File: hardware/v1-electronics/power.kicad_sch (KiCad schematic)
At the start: 33 parts, among them IC3 USBLC6-2SC6, IC4 TPS61288LRQQR, IC5 MP2721GRH-0000-Z, J1 USB_C_Receptacle_USB2.0_14P, J4 Conn_01x02, SW77 SW_Push

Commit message: feat(v1 hardware): select passives values
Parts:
- removed C54: C_Small, symbol Device:C_Small
- added C55: 0.10μF, symbol Device:C_Small
- added C56, C57: 22μF, symbol Device:C_Small
- C27: value 1uF -> 1μF
- C31: value 4.7uF -> 4.7μF
- C34, C48: value 20uF -> 20μF
- C47: value 1uF -> 10μF
- C49: value C_Small -> 0.10μF
- C50: value C_Small -> 10μF
- C51: value C_Small -> 2.20μF
- C52: value C_Small -> 22μF
- C53: value C_Small -> 2.7nF
- L3: value L_Ferrite_Small -> 2.20μH
- L4: value L_Small -> 560nH
- R47, R48: value 5.1k -> 5.1kΩ
- R49, R50, R51, R55: value 10k -> 10kΩ
- R52: value R_Small -> 6kΩ
- R53: value R_Small -> 44kΩ
- R54: value R_Small -> 10kΩ
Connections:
- net V_CHRG is gone; now on net V_IN_TPS: L4.1
- net COMP: now also C53.2; no longer C53.1
- net Earth: now also C55.1, C56.1, C57.1
- net at R54.1: now also C53.1; no longer C53.2
- net V_IN_TPS: now reaches C34.1, C50.2, IC4.7 (VIN), IC5.13 (SYS)
- net V_IN_TPS: now also L3.2, C55.2; no longer L3.1
- net BST_TPS: now reaches IC4.8 (BST)
- net BST_TPS: now also C49.2; no longer C49.1
- net SW_TPS: now reaches IC4.9 (SW_2)
- net SW_TPS: now also C49.1, IC4.4 (SW_1), L3.1
- net BST renamed BST_MP
- net SW renamed SW_MP
- net VOUT renamed V_OUT
- net V_OUT: now also C56.2, C57.2
- no-connect marks 1 -> 0
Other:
- note added: "Did a bunch of math to select a part for this. It resulted in me going with the recommended inductance"
- note added: "Did the math, realized I don't have control system intuition. I have raw values I need to map to stardard resistor and capcitor size and values: - R_C = 14403.29218 Ω - C_C = 2.673 nF - C_P = 6.4152 pF These are the values after plugging in a real output cap (CL21A226MAQNNN): - R_C = 10020.57613 Ω - C_C = 2.673 nF - C_P = 2.88684 pF These are the standard values I'm going with: - R_C = 10 kΩ - C_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"
- note added: "Have not done the math for this yet This involves control theory noise a big issue in these system"
- note added: "Not sure if I should put a capacitor here. TI recommends putting a capacitor across the second resistor(R2) to protect against noise. The criteria is whiether R2 > or < 15kΩ. Though the datasheet has confliciting suggestions between Section 9.2.2.1 and Section 9.2"
- note added: "Set V_out to 5v Datasheet Section 9.2.2.1"
- note added: "This cap needs to be rated for +4A, X7R or X5R of current based on the page 40 of the datasheet. I caculated a max current ripple of about 1.3A"
- note added: "You should use the TPS61288L HotRod Lite variant"
- note added: "based on Datasheet Section 9.2.2.4 used to manage: - voltage ripple - load transient response Watch out for DC Bias injection **optional review **derating is important here Choose this cap: CL21A226MAQNNN"
- note added: "calculations the value of the inductor for our usage is about 509 nH, for part finding perposes 560 nH part."
- moved on the sheet: C46, C47, C49, C53, L3, L4, R52, R53, R54

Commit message: refactor(v1 hardware): convert switch matrix to hierarchical pins
made other changes
had claude generate a script for making the convertion
the references for this file still need to be fixed
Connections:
- net Earth renamed PGND
- net GND renamed DGND
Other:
- title: (none) -> Slack
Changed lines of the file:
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@@
 	(generator_version "10.0")
 	(paper "User" 510 300)
+	(title_block
+		(title "Slack")
+		(date "2026-06-17")
+		(rev "A.0.0")
+	)
 	(rectangle
 		(start 228.6 149.86)
@@
 	)
 	(junction
+		(at 487.68 86.36)
+		(diameter 0)
+		(color 0 0 0 0)
+	)
+	(junction
 		(at 452.12 88.9)
 		(diameter 1.5)
@@
 	)
 	(junction
+		(at 172.72 96.52)
+		(diameter 1.5)
+		(color 0 0 0 0)
+	)
+	(junction
 		(at 299.72 193.04)
 		(diameter 0)
@@
 	(wire
 		(pts
+			(xy 172.72 93.98) (xy 172.72 96.52)
+		)
+		(stroke
+			(width 0.5)
+			(type default)
+		)
+	)
+	(wire
+		(pts
 			(xy 365.76 177.8) (xy 368.3 177.8)
 		)
@@
 	(wire
 		(pts
+			(xy 490.22 86.36) (xy 487.68 86.36)
+		)
+		(stroke
+			(width 0.5)
+			(type default)
+		)
+	)
+	(wire
+		(pts
 			(xy 304.8 167.64) (xy 314.96 167.64)
 		)
@@
 	(wire
 		(pts
+			(xy 487.68 86.36) (xy 487.68 88.9)
+		)
+		(stroke
+			(width 0.5)
+			(type default)
+		)
+	)
+	(wire
+		(pts
 			(xy 457.2 91.44) (xy 457.2 88.9)
 		)
@@
 	(wire
 		(pts
-			(xy 487.68 83.82) (xy 487.68 88.9)
+			(xy 487.68 83.82) (xy 487.68 86.36)
 		)
 		(stroke
@@
 	(wire
 		(pts
-			(xy 50.8 96.52) (xy 251.46 96.52)
+			(xy 50.8 96.52) (xy 172.72 96.52)
 		)
 		(stroke
@@
 	(wire
 		(pts
+			(xy 172.72 96.52) (xy 251.46 96.52)
+		)
+		(stroke
+			(width 0.5)
+			(type default)
+		)
+	)
+	(wire
+		(pts
 			(xy 106.68 66.04) (xy 104.14 66.04)
 		)
@@
 		)
 	)
-	(label "V_BUS"
-		(at 58.42 96.52 0)
-		(effects
-			(font
-				(size 1.27 1.27)
-			)
-			(justify left bottom)
-		)
-	)
 	(label "BST_MP"
 		(at 284.48 99.06 0)
@@
 		)
 	)
-	(global_label "D-"
-		(shape input)
-		(at 165.1 106.68 270)
-		(fields_autoplaced yes)
-		(effects
-			(font
-				(size 1.27 1.27)
-			)
-			(justify right)
-		)
-		(property "Intersheetrefs" "${INTERSHEET_REFS}"
-			(at 165.1 112.5076 90)
-			(hide yes)
-			(show_name no)
-			(do_not_autoplace no)
-			(effects
-				(font
-					(size 1.27 1.27)
-				)
-				(justify right)
-			)
-		)
-	)
 	(global_label "I2C1_SCL"
 		(shape input)
@@
 		)
 	)
-	(global_label "D+"
-		(shape input)
-		(at 160.02 106.68 270)
-		(fields_autoplaced yes)
-		(effects
-			(font
-				(size 1.27 1.27)
-			)
-			(justify right)
-		)
-		(property "Intersheetrefs" "${INTERSHEET_REFS}"
-			(at 160.02 112.5076 90)
-			(hide yes)
-			(show_name no)
-			(do_not_autoplace no)
-			(effects
-				(font
-					(size 1.27 1.27)
-				)
-				(justify right)
-			)
-		)
-	)
 	(global_label "I2C1_SDA"
 		(shape input)
@@
 		)
 	)
+	(hierarchical_label "V_BUS"
+		(shape output)
+		(at 172.72 93.98 90)
+		(effects
+			(font
+				(size 1.27 1.27)
+			)
+			(justify left)
+		)
+	)
+	(hierarchical_label "V_SYS"
+		(shape output)
+		(at 490.22 86.36 0)
+		(effects
+			(font
+				(size 1.27 1.27)
+			)
+			(justify left)
+		)
+	)
+	(hierarchical_label "D+"
+		(shape bidirectional)
+		(at 160.02 106.68 270)
+		(effects
+			(font
+				(size 1.27 1.27)
+			)
+			(justify right)
+		)
+	)
+	(hierarchical_label "D-"
+		(shape bidirectional)
+		(at 165.1 106.68 270)
+		(effects
+			(font
+				(size 1.27 1.27)
+			)
+			(justify right)
+		)
+	)
 	(symbol
 		(lib_id "Device:L_Small")
@@
 			)
 		)
-		(property "Value" "Earth"
+		(property "Value" "PGND"
 			(at 370.84 114.3 0)
 			(show_name no)
@@
 			)
 		)
-		(property "Value" "GND"
+		(property "Value" "DGND"
 			(at 35.5599 138.43 0)
 			(show_name no)
@@
 			)
 		)
-		(property "Value" "Earth"
+		(property "Value" "PGND"
 			(at 269.24 226.06 0)
 			(show_name no)
@@
 			)
 		)
-		(property "Value" "GND"
+		(property "Value" "DGND"
 			(at 271.78 137.16 0)
 			(show_name no)
@@
 			)
 		)
-		(property "Value" "Earth"
+		(property "Value" "PGND"
 			(at 477.52 101.6 0)
 			(show_name no)
@@
 			)
 		)
-		(property "Value" "GND"
+		(property "Value" "DGND"
 			(at 414.02 127 0)
 			(show_name no)
@@
 			)
 		)
-		(property "Value" "GND"
+		(property "Value" "DGND"
 			(at 50.8 156.2099 0)
 			(show_name no)
@@
 			)
 		)
-		(property "Value" "Earth"
+		(property "Value" "PGND"
 			(at 274.32 142.24 0)
 			(show_name no)
@@
 			)
 		)
-		(property "Value" "GND"
+		(property "Value" "DGND"
 			(at 88.8999 87.63 0)
 			(show_name no)
@@
 			)
 		)
-		(property "Value" "Earth"
+		(property "Value" "PGND"
 			(at 457.2 101.6 0)
 			(show_name no)
@@
 			)
 		)
-		(property "Value" "Earth"
+		(property "Value" "PGND"
 			(at 314.96 200.66 0)
 			(show_name no)
@@
 			)
 		)
-		(property "Value" "GND"
+		(property "Value" "DGND"
 			(at 294.64 180.34 0)
 			(show_name no)
@@
 			)
 		)
-		(property "Value" "Earth"
+		(property "Value" "PGND"
 			(at 467.36 101.6 0)
 			(show_name no)
@@
 			)
 		)
-		(property "Value" "Earth"
+		(property "Value" "PGND"
 			(at 396.24 114.3 0)
 			(show_name no)
@@
 			)
 		)
-		(property "Value" "GND"
+		(property "Value" "DGND"
 			(at 426.72 121.92 0)
 			(show_name no)
@@
 			)
 		)
-		(property "Value" "Earth"
+		(property "Value" "PGND"
 			(at 299.72 203.2 0)
 			(show_name no)
@@
 			)
 		)
-		(property "Value" "Earth"
+		(property "Value" "PGND"
 			(at 309.88 114.3 0)
 			(show_name no)
@@
 			)
 		)
-		(property "Value" "GND"
+		(property "Value" "DGND"
 			(at 441.96 175.26 0)
 			(show_name no)
@@
 			)
 		)
-		(property "Value" "GND"
+		(property "Value" "DGND"
 			(at 281.94 199.3899 0)
 			(show_name no)
@@
 			)
 		)
-		(property "Value" "GND"
+		(property "Value" "DGND"
 			(at 403.86 182.88 0)
 			(show_name no)
@@
 			)
 		)
-		(property "Value" "Earth"
+		(property "Value" "PGND"
 			(at 419.1 121.92 0)
 			(show_name no)
@@
 			)
 		)
-		(property "Value" "GND"
+		(property "Value" "DGND"
 			(at 243.84 214.6299 0)
 			(show_name no)
@@
 			)
 		)
-		(property "Value" "Earth"
+		(property "Value" "PGND"
 			(at 266.7 180.34 0)
 			(show_name no)
@@
 			)
 		)
-		(property "Value" "GND"
+		(property "Value" "DGND"
 			(at 27.9399 138.43 0)
 			(show_name no)

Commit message: refactor(v1 hardware): all sheets now use hierarchical labels
We'll might change these to buses down the line, but we'll see
I'm happy for now
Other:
- note added: "SHould this be on PGND?"
- note removed: "Input Decoupler"
- moved on the sheet: C47

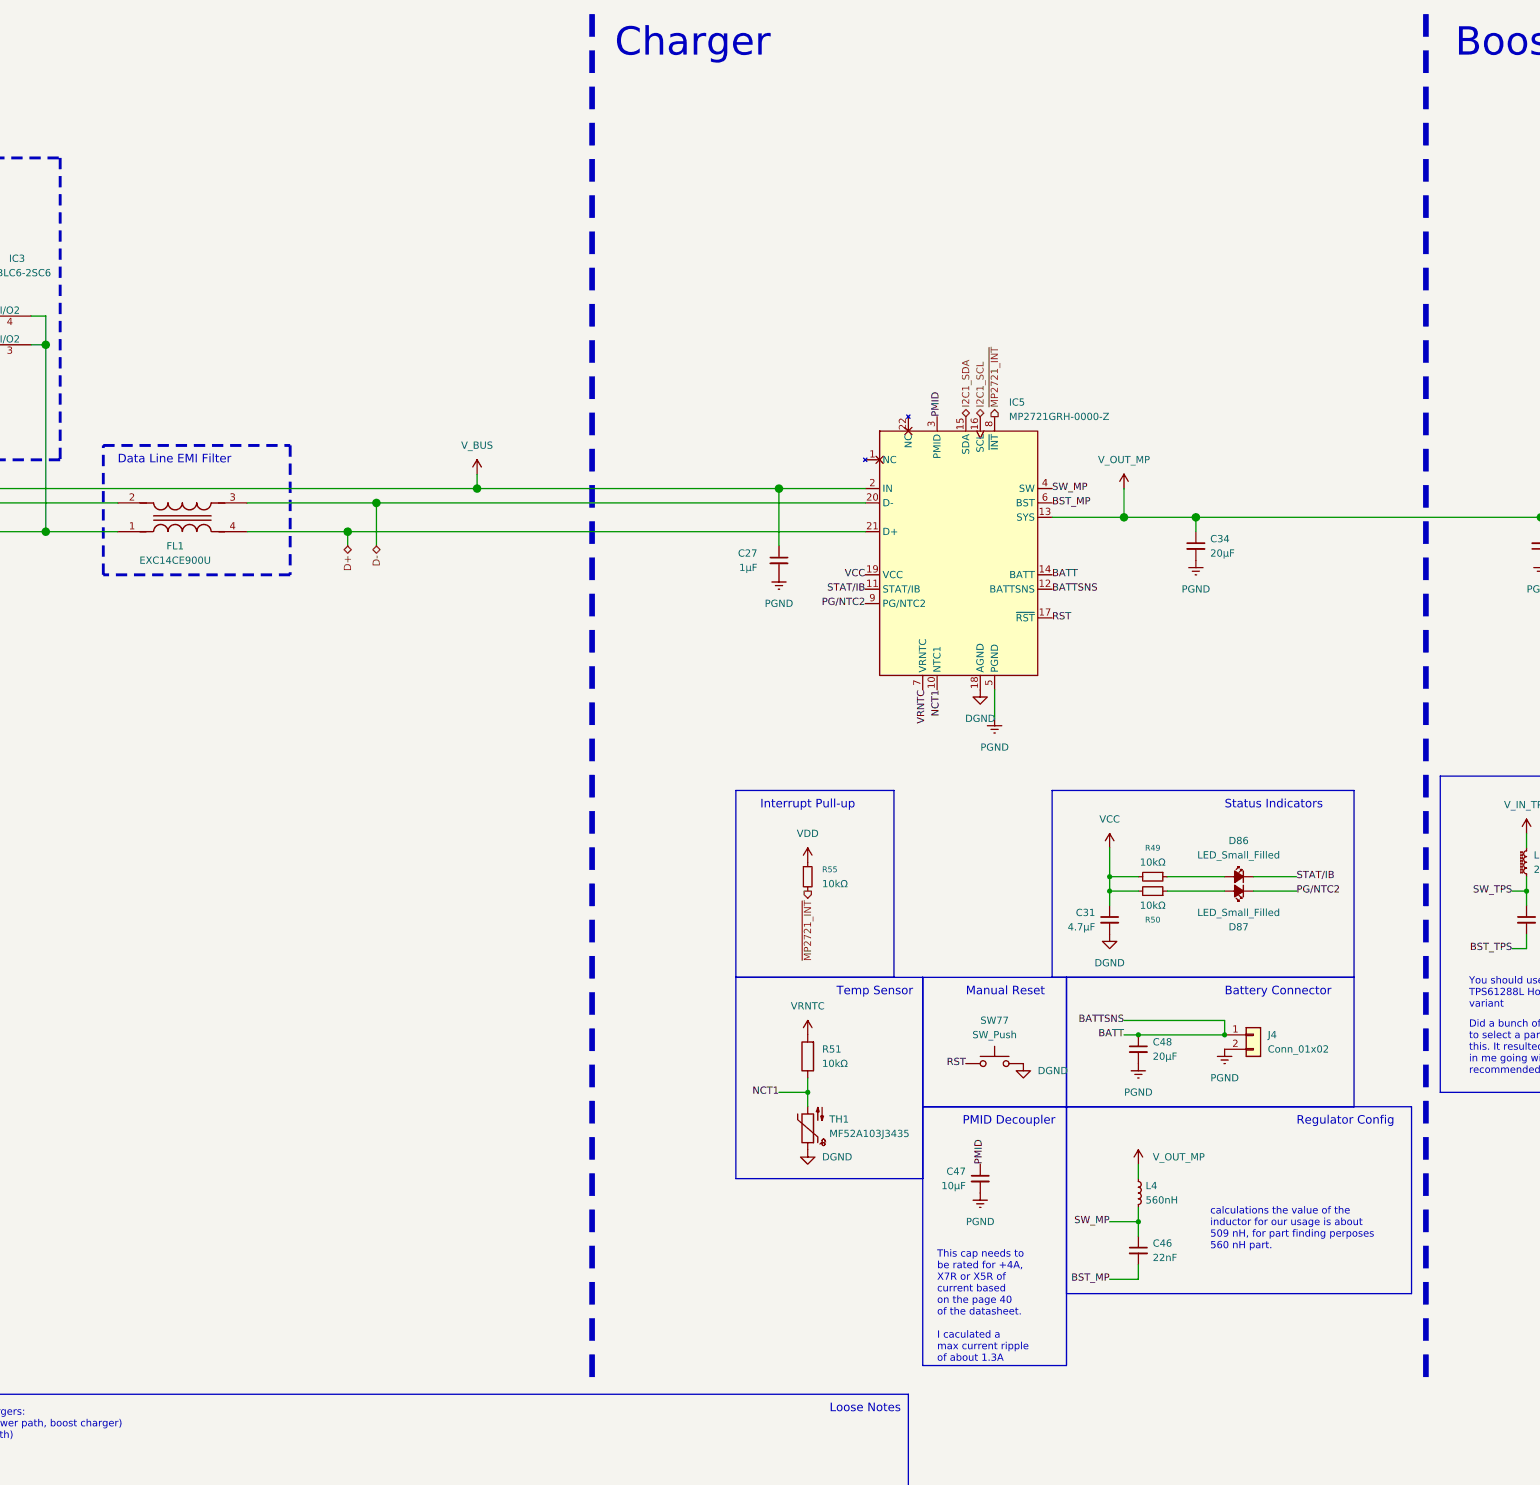
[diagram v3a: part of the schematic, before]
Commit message: refactor(v1 hardware): root level schematic is made discriptive with hierarchical pins
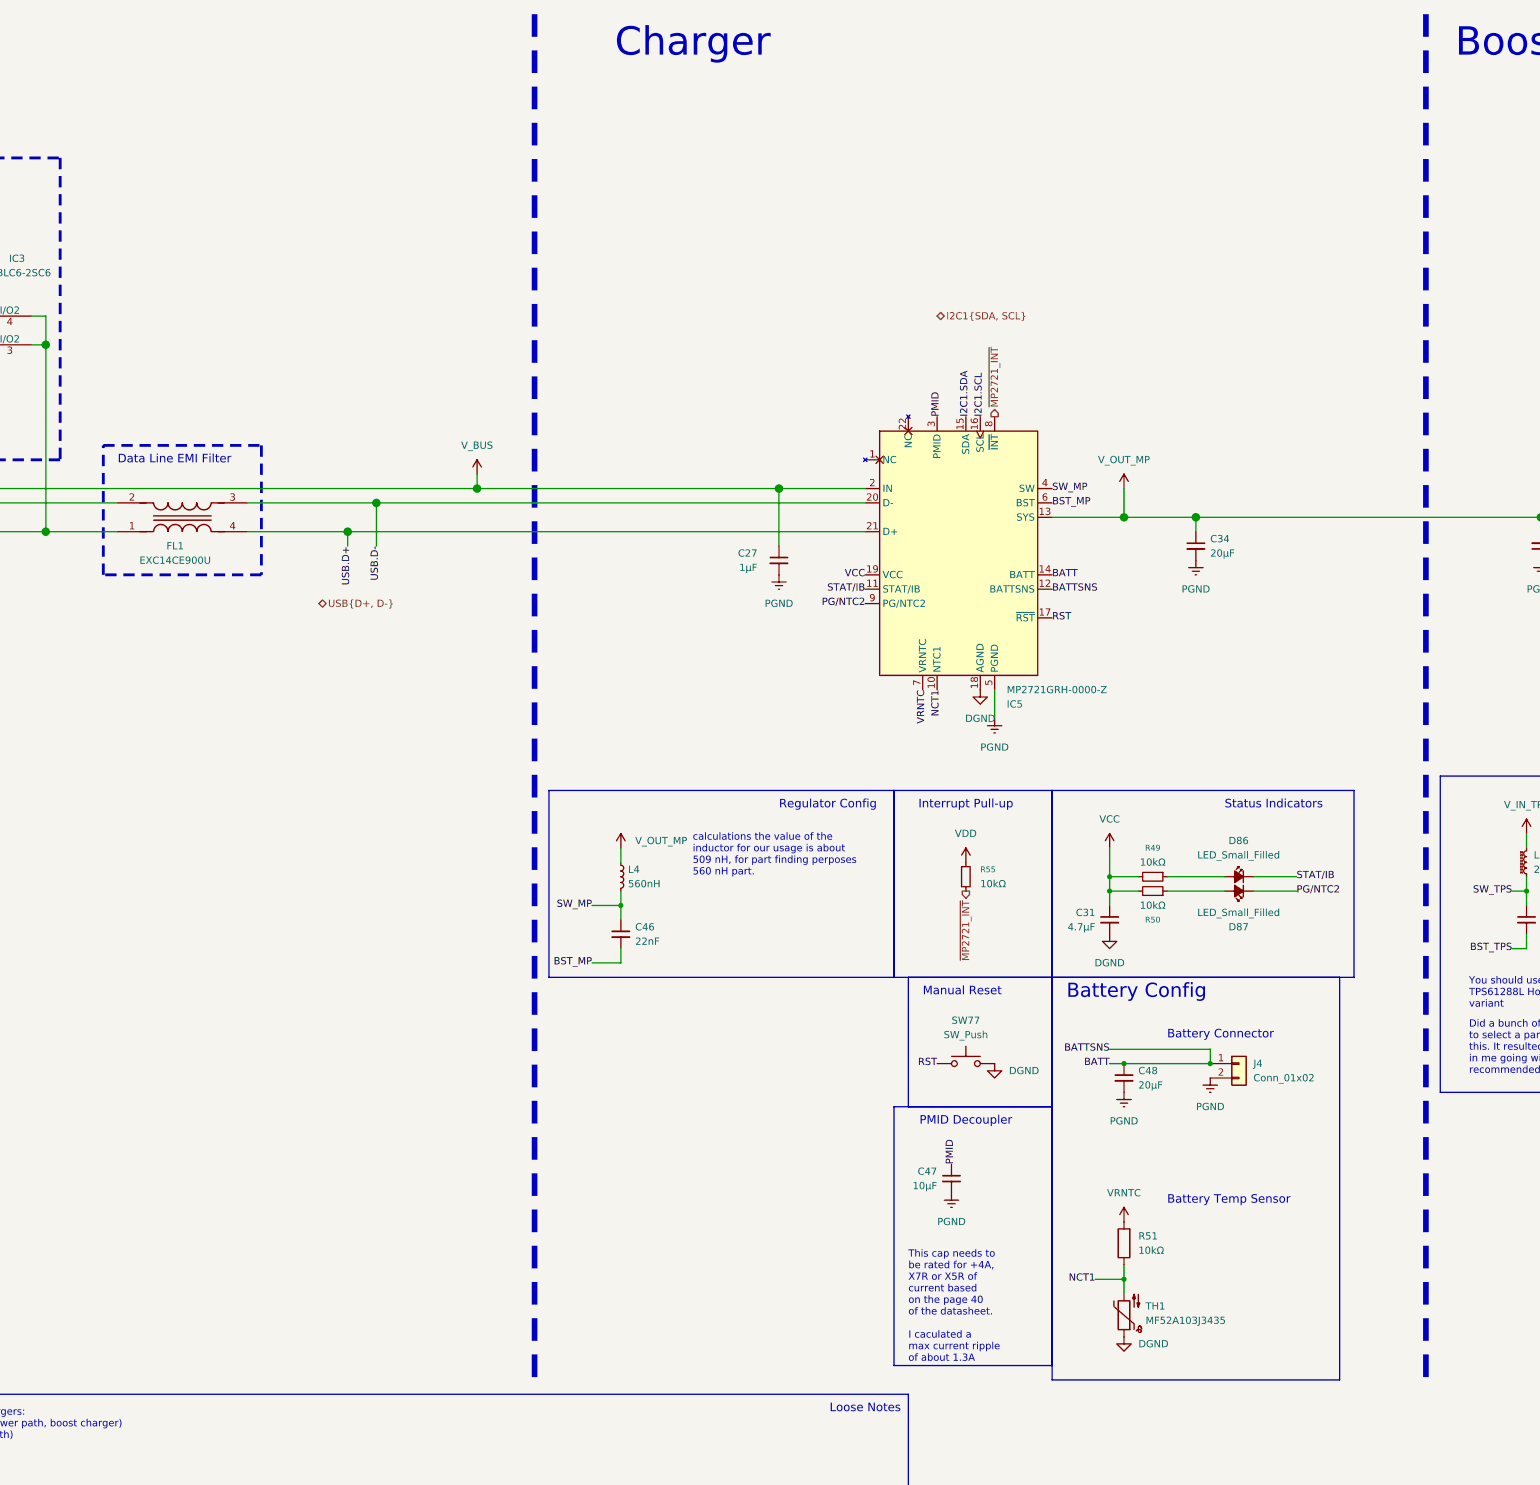
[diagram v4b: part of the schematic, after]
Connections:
- net D+ renamed USB.D+
- net D- renamed USB.D-
- net I2C1_SCL renamed I2C1.SCL
- net I2C1_SDA renamed I2C1.SDA
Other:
- note added: "Battery Config"
- note added: "Battery Temp Sensor"
- note removed: "Temp Sensor"
- moved on the sheet: C46, C47, C48, J4, L4, R51, R55, SW77, TH1

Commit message: refactor(v1 hardware): get references in order
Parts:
- removed IC3: USBLC6-2SC6, SOT95P280X145-6N, symbol STMicroelectronics:USBLC6-2SC6
- removed SW77: SW_Push, symbol Switch:SW_Push
- added D64: USBLC6-2SC6, SOT95P280X145-6N, symbol STMicroelectronics:USBLC6-2SC6
- added SW7: SW_Push, symbol Switch:SW_Push
- J1: value USB_C_Receptacle_USB2.0_14P -> Female USB-C USB2.0
- J2: renamed from J4; value Conn_01x02 -> Female JST-SH
- renumbered C56 to C37, C52 to C38, C57 to C39, C34 to C40, C50 to C41, C55 to C42, C27 to C43, C51 to C44, C53 to C45, C31 to C46, C46 to C47, C49 to C48, C47 to C49, C48 to C50, D86 to D65, D87 to D86, IC4 to IC1, IC5 to IC2, L4 to L1, L3 to L2, R47 to R49, R53 to R50, R48 to R51, R49 to R52, R50 to R53, R55 to R54, R52 to R55, R54 to R56, R51 to R57
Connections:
- net TPS61288_EN is gone; now on net V_IN_TPS: IC1.6 (EN)
- net DGND: now also D64.2 (GND)
- net V_BUS: now also D64.5 (VBUS)
- net V_IN_TPS: now also SW7.2; no longer C40.1, IC2.13 (SYS), L1.1
- net ~{MP2721_INT}: no longer R54.2
- net at J1.A7 (D-), J1.B7 (D-): now also D64.1 (I/O1); no longer FL1.2
- net at J1.A6 (D+), J1.B6 (D+): now also D64.3 (I/O2); no longer FL1.1
- net RST: no longer names the net of IC2.17 (~{RST})
- new net: D64.4 (I/O2), FL1.1
- new net: D64.6 (I/O1), FL1.2
- new net V_OUT_MP: C40.1, IC2.13 (SYS), L1.1, SW7.1
- new net ~{INT}: R54.2
- no-connect marks 0 -> 1
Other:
- note added: "*set to always on. trying to control this would be a power squencing nightmare"
- note added: "On/Off Switch"
- note added: "Should this be on PGND?"
- note removed: "Manual Reset"
- note removed: "SHould this be on PGND?"
- moved on the sheet: C44, C45, C46, C47, C48, C49, C50, D65, D86, J2, L1, L2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
